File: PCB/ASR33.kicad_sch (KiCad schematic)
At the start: 42 parts, among them J1 USB-C, J2 DC, J3 Power, J4 RUN, J5 Tx, J6 Rx, Q1 NX7002AK, SW1 SW_Push, U1 ESP32-PICO-MINI-02, U2 FT231XQ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

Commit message: Production files
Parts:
- removed J1: USB-C, RevK:USC16-TR, symbol RevK:USB-C
- added J7: USB-C, RevK:USC16-TR, symbol RevK:USB-C
- D2, D3, U3, U4, U5: JLCPCB Rotation Offset (none) -> -90
- D4: LCSC Part # (none) -> C143805
- Q1: JLCPCB Rotation Offset (none) -> 180
- U2: LCSC Part # (none) -> C132159
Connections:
- net GND: now also J7.A1 (GND), J7.A12 (GND), J7.B1 (GND), J7.B12 (GND), J7.S1 (SHIELD)
- net VBUS: now also J7.A4 (VBUS), J7.A9 (VBUS), J7.B4 (VBUS), J7.B9 (VBUS)
- net at R7.1: now also J7.A5 (CC1)
- net at R8.2: now also J7.B5 (CC2)
- net at C2.1, R9.1: now also J7.A7 (D-), J7.B7 (D-)
- net at C3.1, R10.2: now also J7.A6 (D+), J7.B6 (D+)

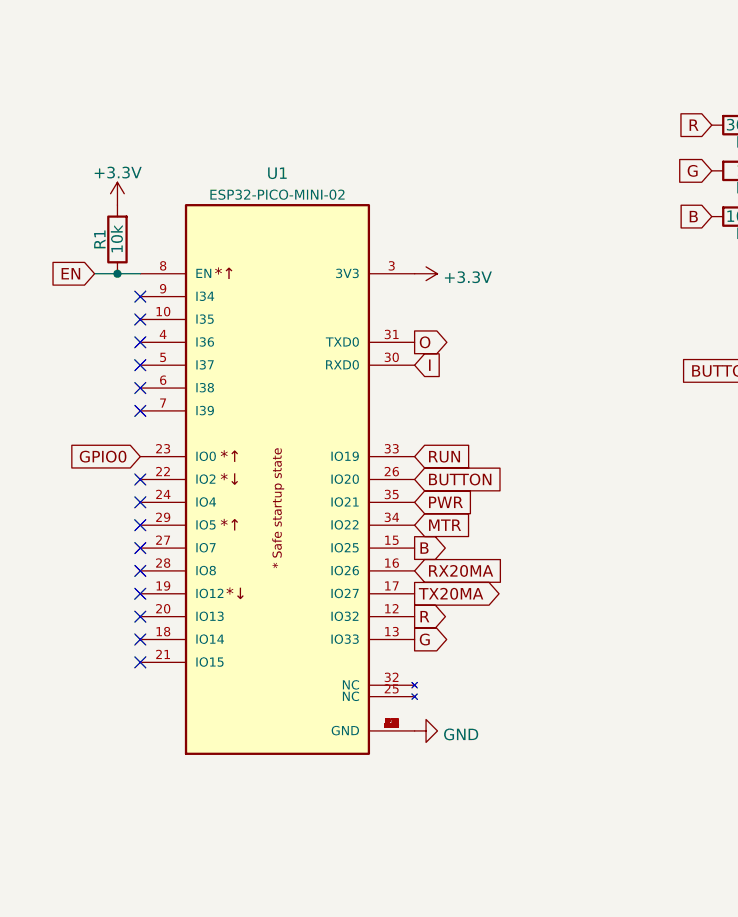
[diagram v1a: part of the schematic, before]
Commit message: Added programming header for when not using USB data
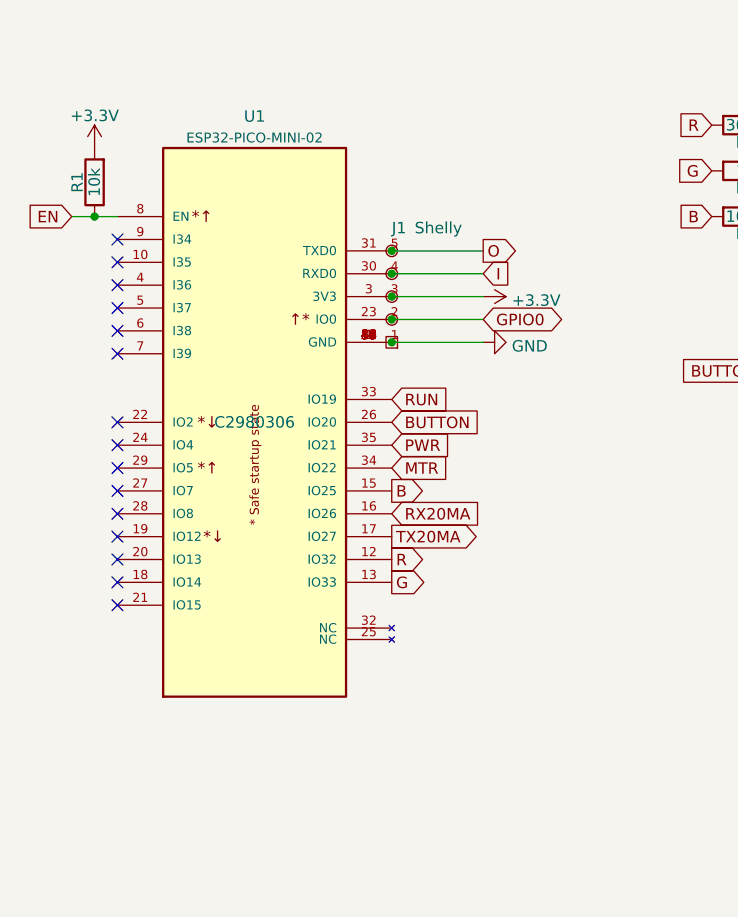
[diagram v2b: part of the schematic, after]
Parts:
- added J1: Shelly, RevK:Shelly, symbol RevK:Shelly
- U1: LCSC Part # (none) -> C2980306
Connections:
- net +3V3: now also J1.3 (3V3)
- net GND: now also J1.1 (GND)
- net GPIO0: now also J1.2 (0)
- net I: now also J1.4 (Rx)
- net O: now also J1.5 (Tx)
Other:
- moved on the sheet: R1, U1

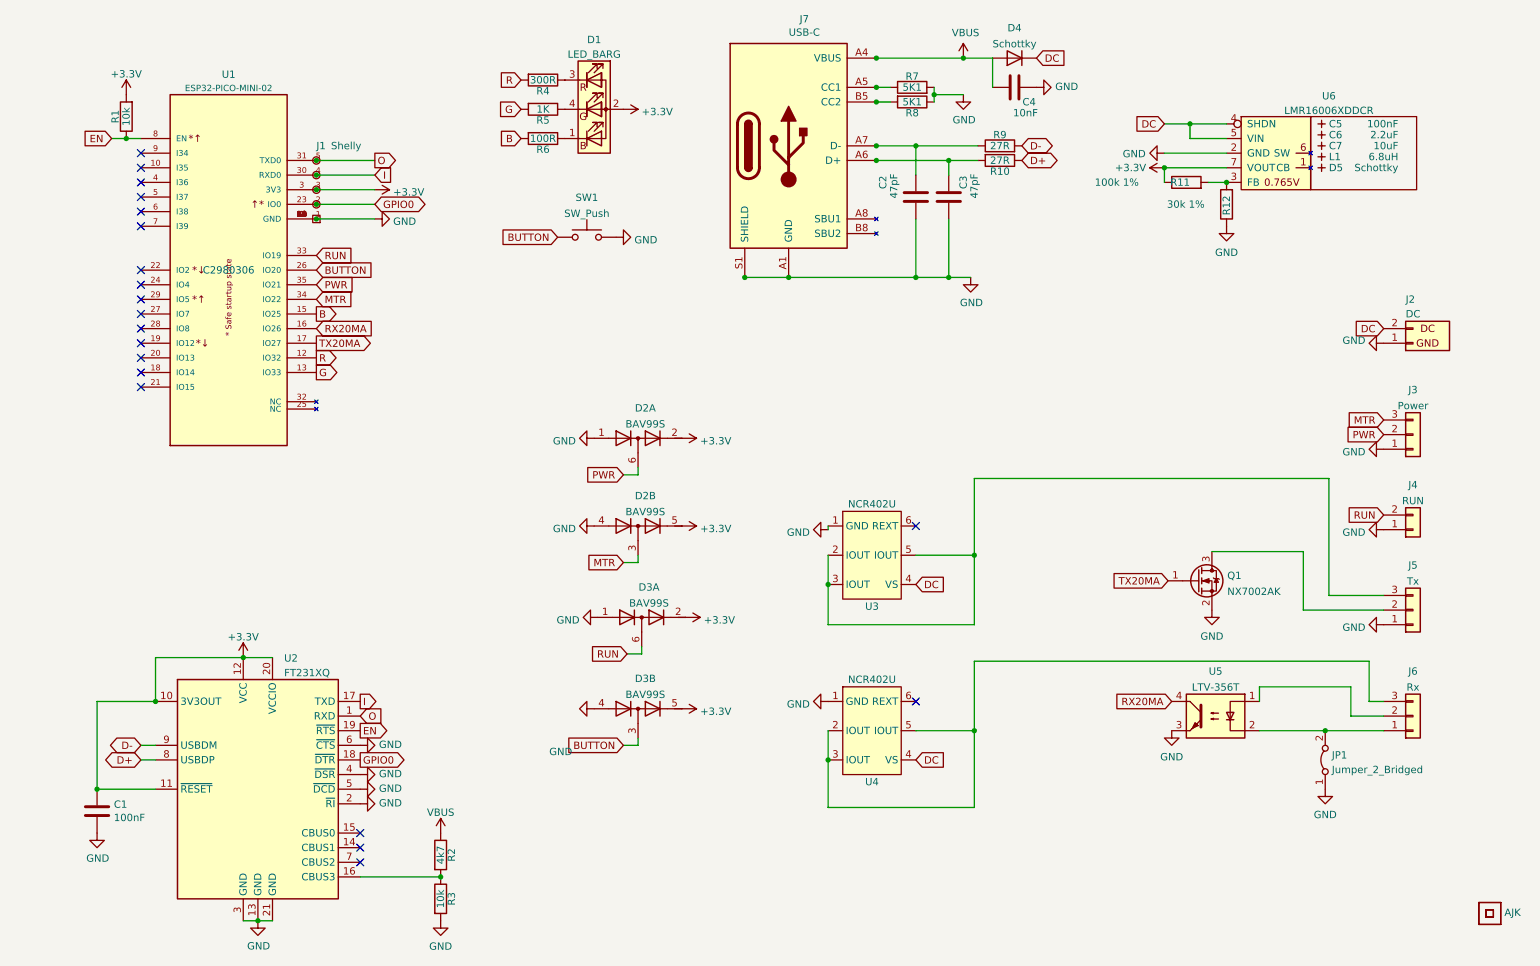
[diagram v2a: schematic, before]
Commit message: Rework for 5 pin header instead of USB/USART
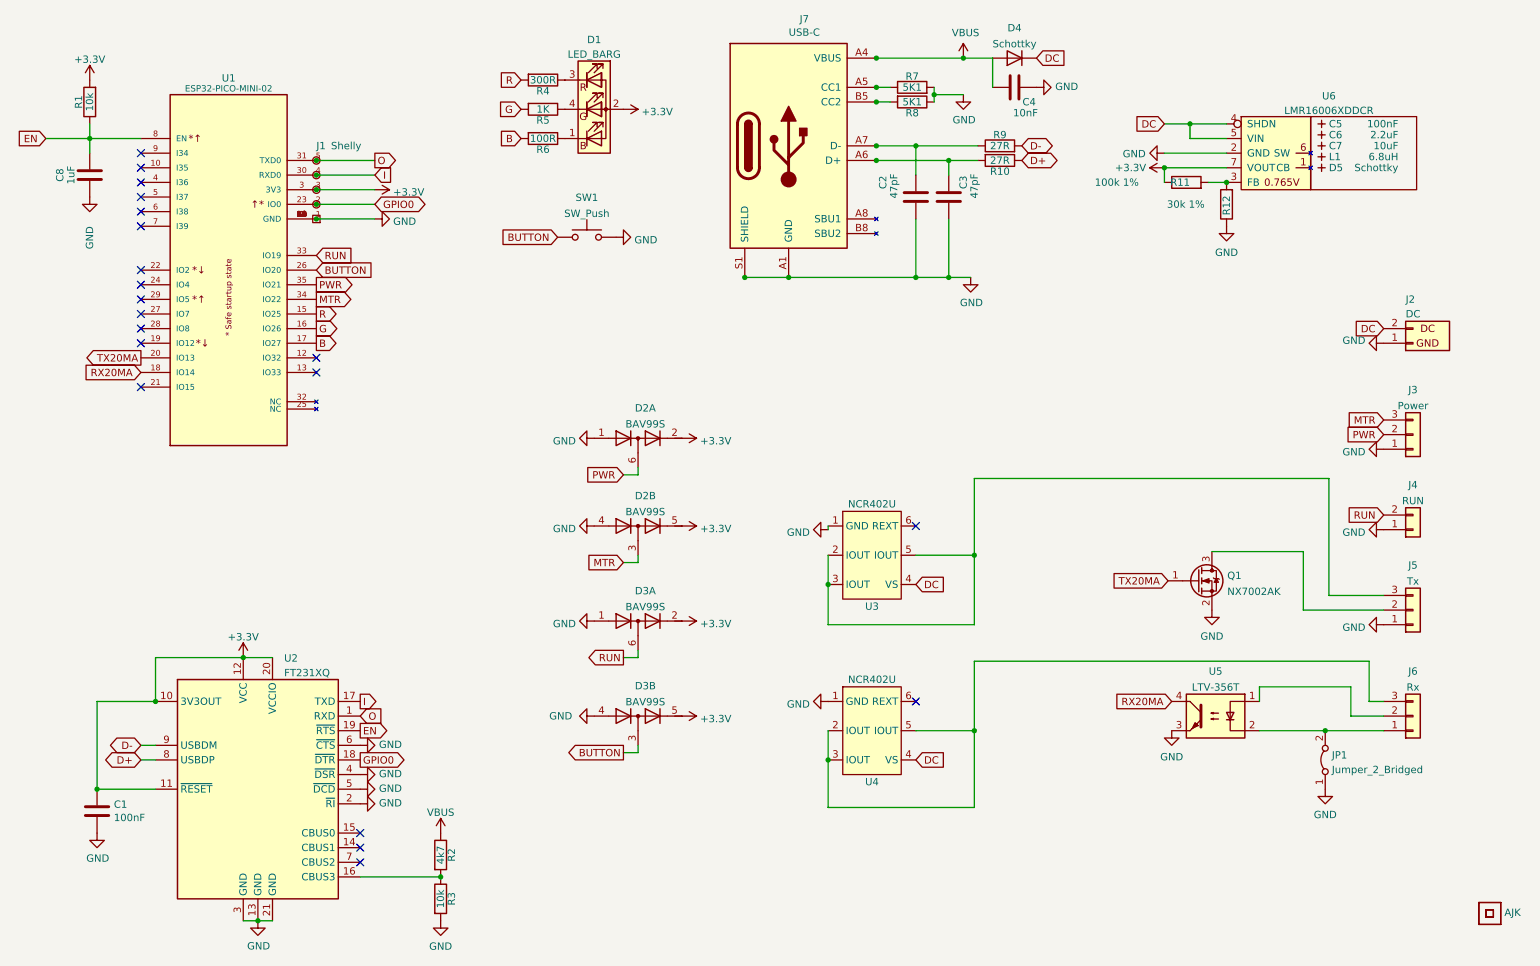
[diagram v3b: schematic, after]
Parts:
- added C8: 1uF, RevK:C_0603, symbol Device:C
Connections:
- net B: now also U1.17 (IO27); no longer U1.15 (IO25)
- net EN: now also C8.2
- net G: now also U1.16 (IO26); no longer U1.13 (IO33)
- net GND: now also C8.1
- net R: now also U1.15 (IO25); no longer U1.12 (IO32)
- net RX20MA: now also U1.18 (IO14); no longer U1.16 (IO26)
- net TX20MA: now also U1.20 (IO13); no longer U1.17 (IO27)
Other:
- moved on the sheet: D3A, D3B, R1

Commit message: Tidy silk
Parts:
- D5: JLCPCB Rotation Offset 0 -> (none)
- Q1: footprint Package_TO_SOT_SMD:SOT-23 -> RevK:SOT-23
- U5: footprint Package_SO:SO-4_4.4x3.6mm_P2.54mm -> RevK:SO-4_4.4x3.6mm_P2.54mm
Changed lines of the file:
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@@
   (symbol (lib_id "Device:R") (at 231.775 50.8 180) (unit 1)
     (in_bom yes) (on_board yes) (dnp no)
-    (property "Reference" "R12" (at 231.775 52.705 90)
-      (effects (font (size 1.27 1.27)) (justify right))
-    )
-    (property "Value" "30k 1%" (at 227.965 50.8 0)
+    (property "Reference" "R12" (at 231.775 50.8 90)
+      (effects (font (size 1.27 1.27)))
+    )
+    (property "Value" "30k 1%" (at 229.87 47.625 90)
       (effects (font (size 1.27 1.27)) (justify left))
     )
@@
       (effects (font (size 1.27 1.27)))
     )
-    (property "Footprint" "Package_SO:SO-4_4.4x3.6mm_P2.54mm" (at 234.95 144.78 0)
+    (property "Footprint" "RevK:SO-4_4.4x3.6mm_P2.54mm" (at 234.95 144.78 0)
       (effects (font (size 1.27 1.27) italic) (justify left) hide)
     )
@@
       (effects (font (size 1.27 1.27)) (justify left))
     )
-    (property "Footprint" "Package_TO_SOT_SMD:SOT-23" (at 231.775 113.665 0)
+    (property "Footprint" "RevK:SOT-23" (at 231.775 113.665 0)
       (effects (font (size 1.27 1.27)) hide)
     )
@@
   (symbol (lib_id "Device:R") (at 224.79 46.99 90) (unit 1)
     (in_bom yes) (on_board yes) (dnp no)
-    (property "Reference" "R11" (at 225.425 46.99 90)
-      (effects (font (size 1.27 1.27)) (justify left))
-    )
-    (property "Value" "100k 1%" (at 216.535 46.99 90)
+    (property "Reference" "R11" (at 224.79 46.99 90)
+      (effects (font (size 1.27 1.27)))
+    )
+    (property "Value" "100k 1%" (at 227.965 48.895 90)
       (effects (font (size 1.27 1.27)) (justify left))
     )
@@
       (effects (font (size 1.27 1.27)) hide)
     )
-    (property "JLCPCB Rotation Offset" "0" (at 248.285 44.45 0)
-      (effects (font (size 1.27 1.27)) hide)
-    )
